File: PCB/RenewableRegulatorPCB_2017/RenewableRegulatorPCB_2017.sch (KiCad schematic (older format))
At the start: 34 parts, among them J1 JACK_TRS_6PINS, J2 Arduino_Nano_Header, P1 INPUT, P2 Vref?, P3 MicroSD, P4 A6_7, P5 OUTPUT, P6 SERIAL, P7 A2, P8 TP_Vin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

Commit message: Secod
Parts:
- C3: footprint REInnovationFootprint:C_1V7_TH -> RenewableRegulatorPCB_2017_Library_Yoan:Capacitor_C_1V7_TH
- EN1: footprint ~ -> (none)
- P1, P5: footprint matts_components:SIL-2_screw_terminal_32A -> RenewableRegulatorPCB_2017_Library_Yoan:Connecteurs_IO_SIL-2_screw_terminal_32A
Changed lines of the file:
@@
 LIBS:device
 LIBS:conn
+LIBS:RenewableRegulatorPCB_2017
 LIBS:RenewableRegulatorPCB_2017-cache
 EELAYER 25 0
@@
 F 0 "P1" V 1350 1600 40  0000 C CNN
 F 1 "INPUT" V 1450 1600 40  0000 C CNN
-F 2 "matts_components:SIL-2_screw_terminal_32A" H 1400 1600 60  0001 C CNN
+F 2 "RenewableRegulatorPCB_2017_Library_Yoan:Connecteurs_IO_SIL-2_screw_terminal_32A" H 1400 1600 60  0001 C CNN
 F 3 "" H 1400 1600 60  0001 C CNN
 	1    1400 1600
@@
 F 0 "P5" V 10200 1750 40  0000 C CNN
 F 1 "OUTPUT" V 10300 1750 40  0000 C CNN
-F 2 "matts_components:SIL-2_screw_terminal_32A" H 10250 1750 60  0001 C CNN
+F 2 "RenewableRegulatorPCB_2017_Library_Yoan:Connecteurs_IO_SIL-2_screw_terminal_32A" H 10250 1750 60  0001 C CNN
 F 3 "" H 10250 1750 60  0001 C CNN
 	1    10250 1750
@@
 F 0 "C3" H 8925 1650 50  0000 L CNN
 F 1 "100uf" H 8925 1450 50  0000 L CNN
-F 2 "REInnovationFootprint:C_1V7_TH" H 8938 1400 50  0001 C CNN
-F 3 "" H 8900 1550 50  0000 C CNN
+F 2 "RenewableRegulatorPCB_2017_Library_Yoan:Capacitor_C_1V7_TH" H 8938 1400 400 0001 C CNN
+F 3 "" H 8900 1550 400 0001 C CNN
 F 4 "~" H 8900 1550 60  0000 C CNN "Notes"
 F 5 "100V Electrolytic" H 8900 1550 60  0001 C CNN "Description"
 F 6 "Panasonic" H 8900 1550 60  0001 C CNN "Manufacturer"
-F 7 "ECA-2AM101B" H 8900 1550 60  0001 C CNN "Manufacturer Part No"
+F 7 "ECA-2AM101B" H 8900 1550 394 0001 C CNN "Manufacturer Part No"
 F 8 "RS" H 8900 1550 60  0001 C CNN "Supplier 1"
 F 9 "807-3431" H 8900 1550 60  0001 C CNN "Supplier 1 Part No"
@@
 F 0 "EN1" H 6530 6500 40  0000 L CNN
 F 1 "PCB" H 6450 6555 30  0001 C CNN
-F 2 "~" H 6450 6500 60  0001 C CNN
+F 2 "" H 6450 6500 60  0001 C CNN
 F 3 "http://cpc.farnell.com/hammond/1590bb/box-diecast-119x94x30/dp/EN82042?ost=EN82042&selectedCategoryId=&categoryNameResp=All&searchView=table&iscrfnonsku=false" H 6450 6500 60  0001 C CNN
 F 4 "~" H 6450 6500 60  0000 C CNN "Notes"

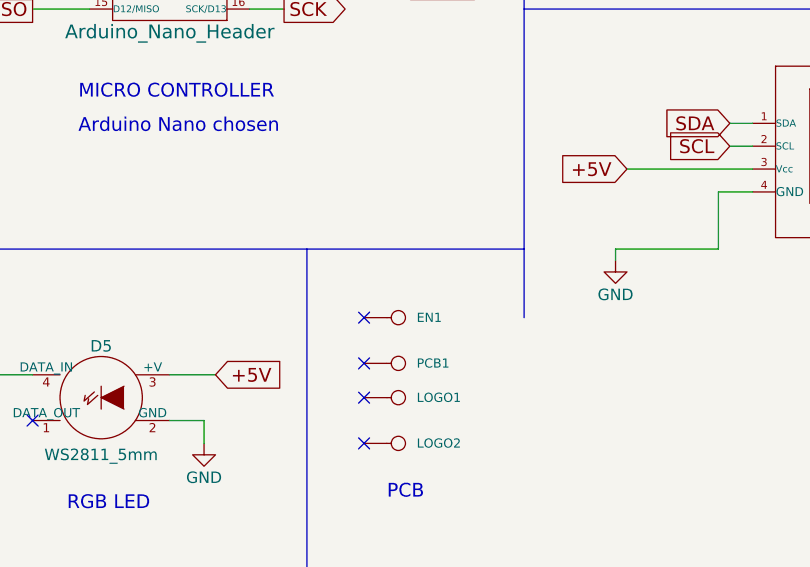
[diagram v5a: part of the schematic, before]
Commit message: Added MH and footprints
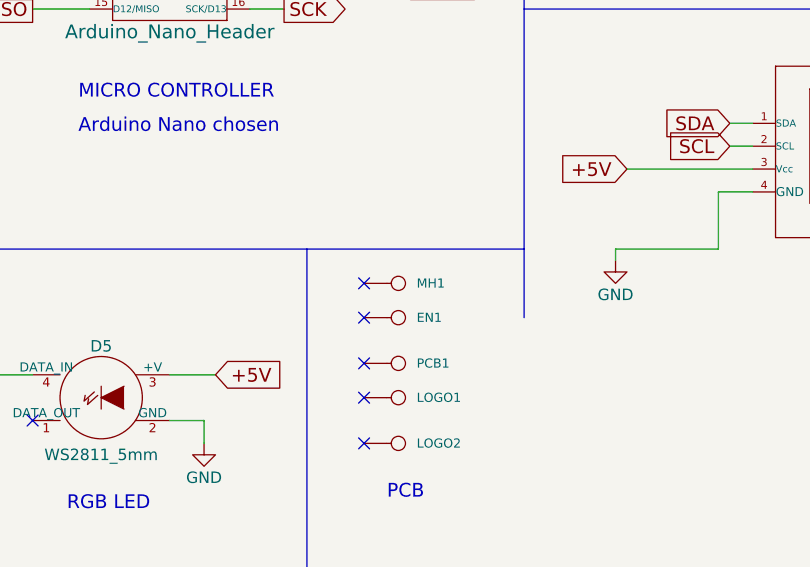
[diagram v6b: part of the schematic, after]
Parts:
- added MH1: Mounting holes, symbol CONN_1
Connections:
- no-connect marks 6 -> 7
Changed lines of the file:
@@
 LIBS:power
 LIBS:device
+LIBS:matts_components
 LIBS:conn
 LIBS:RenewableRegulatorPCB_2017
@@
 	1    0    0    -1
 $EndComp
+NoConn ~ 6300 6350
+$Comp
+L CONN_1 MH1
+U 1 1 58EBB61E
+P 6450 6350
+F 0 "MH1" H 6530 6350 40  0000 L CNN
+F 1 "Mounting holes" H 6450 6405 30  0001 C CNN
+F 2 "" H 6450 6350 60  0001 C CNN
+F 3 "" H 6450 6350 60  0001 C CNN
+F 4 "~" H 6450 6350 60  0000 C CNN "Notes"
+F 5 "4 x M3 mounting holes" H 6450 6350 60  0001 C CNN "Description"
+F 6 "~" H 6450 6350 60  0001 C CNN "Manufacturer"
+F 7 "~" H 6450 6350 60  0001 C CNN "Manufacturer Part No"
+F 8 "~" H 6450 6350 60  0001 C CNN "Supplier 1"
+F 9 "~" H 6450 6350 60  0001 C CNN "Supplier 1 Part No"
+F 10 "~" H 6450 6350 60  0001 C CNN "Supplier 1 Cost"
+F 11 "~" H 6450 6350 60  0001 C CNN "Supplier 2"
+F 12 "~" H 6450 6350 60  0001 C CNN "Supplier 2 Part No"
+F 13 "~" H 6450 6350 60  0001 C CNN "Supplier 2 Cost"
+	1    6450 6350
+	1    0    0    -1
+$EndComp

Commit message: Third Version of PCB
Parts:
- P1, P5: symbol CONN_2 -> CONN_2-RESCUE-RenewableRegulatorPCB_2017
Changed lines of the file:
@@
 LIBS:power
 LIBS:device
-LIBS:matts_components
 LIBS:conn
 LIBS:RenewableRegulatorPCB_2017
@@
 $EndComp
 $Comp
-L CONN_2 P1
+L CONN_2-RESCUE-RenewableRegulatorPCB_2017 P1
 U 1 1 50D3652B
 P 1400 1600
@@
 Reverse Polarity Protection\nWill blow control fuse if reversed.
 $Comp
-L CONN_2 P5
+L CONN_2-RESCUE-RenewableRegulatorPCB_2017 P5
 U 1 1 58E5328E
 P 10250 1750

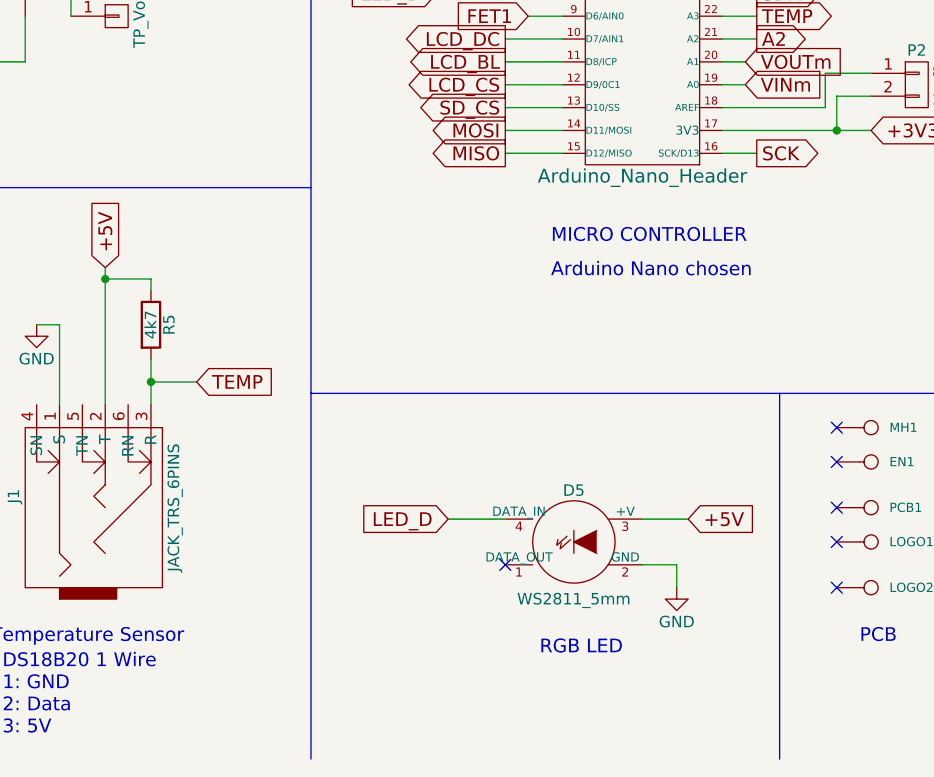
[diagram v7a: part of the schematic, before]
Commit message: Updated PCB and schematic
WS2811 LED swapped around Vcc and GND
OLED swapped around for front mounting
Tracks cleaned up
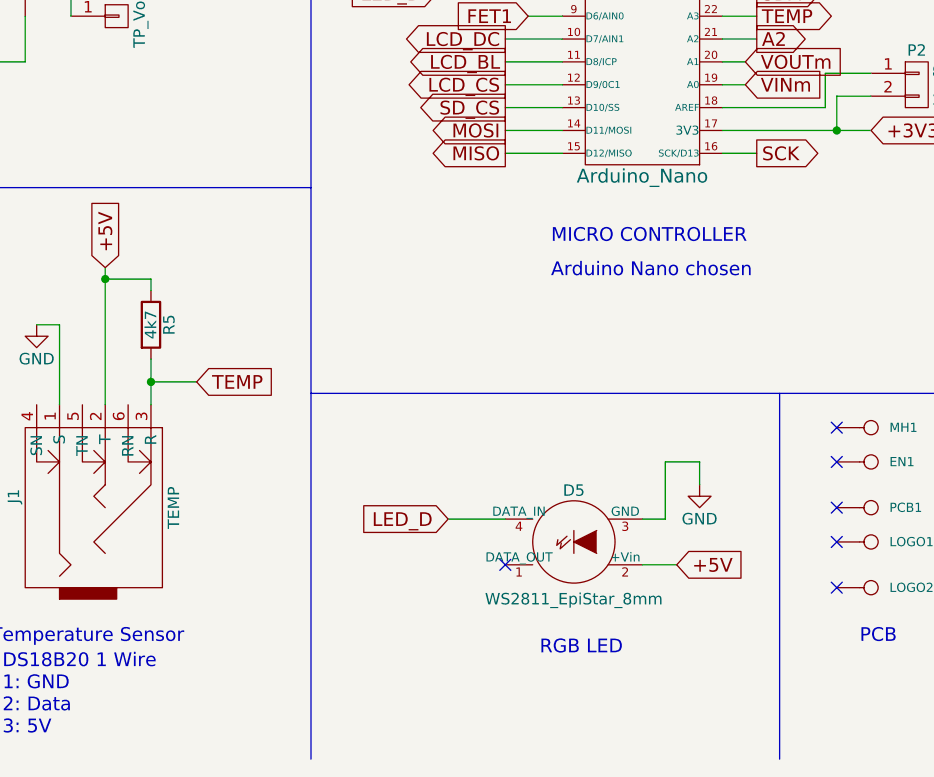
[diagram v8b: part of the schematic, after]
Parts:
- removed D5: WS2811_5mm, REInnovationFootprint:TH_WS2811_LED_8mm, symbol WS2811_5mm
- added D5: WS2811_EpiStar_8mm, REInnovationFootprint:TH_WS2811_LED_8mm, symbol WS2811_EpiStar_8mm
- J1: value JACK_TRS_6PINS -> TEMP
- J2: value Arduino_Nano_Header -> Arduino_Nano
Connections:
- net +5V: now also D5.2 (+Vin)
- net GND: now also D5.3 (GND)
- net LED_D: now also D5.4 (DATA_IN)
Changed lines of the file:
@@
 LIBS:conn
 LIBS:RenewableRegulatorPCB_2017
+LIBS:matts_components
 LIBS:RenewableRegulatorPCB_2017-cache
 EELAYER 25 0
@@
 P 5450 4450
 F 0 "J2" H 5450 5250 60  0000 C CNN
-F 1 "Arduino_Nano_Header" H 5450 3650 60  0000 C CNN
+F 1 "Arduino_Nano" H 5450 3650 60  0000 C CNN
 F 2 "REInnovationFootprint:NANO_DIP_30_600" H 5450 4450 60  0001 C CNN
 F 3 "" H 5450 4450 60  0000 C CNN
@@
 	1    0    0    -1
 $EndComp
-$Comp
-L WS2811_5mm D5
-U 1 1 58E3F557
-P 5150 6850
-F 0 "D5" H 5150 7075 50  0000 C CNN
-F 1 "WS2811_5mm" H 5150 6600 50  0000 C CNN
-F 2 "REInnovationFootprint:TH_WS2811_LED_8mm" H 5150 6850 50  0001 C CNN
-F 3 "https://www.coolcomponents.co.uk/en/opto/leds/digital-rgb-addressable-led-5mm-through-hole-10-pack.html" H 5150 6850 50  0001 C CNN
-F 4 "~" H 5150 6850 60  0000 C CNN "Notes"
-F 5 "TH WS2811 Single LED Addressable" H 5150 6850 60  0001 C CNN "Description"
-F 6 "~" H 5150 6850 60  0001 C CNN "Manufacturer"
-F 7 "~" H 5150 6850 60  0001 C CNN "Manufacturer Part No"
-F 8 "AliExpress" H 5150 6850 60  0001 C CNN "Supplier 1"
-F 9 "~" H 5150 6850 60  0001 C CNN "Supplier 1 Part No"
-F 10 "~" H 5150 6850 60  0001 C CNN "Supplier 1 Cost"
-F 11 "~" H 5150 6850 60  0001 C CNN "Supplier 2"
-F 12 "~" H 5150 6850 60  0001 C CNN "Supplier 2 Part No"
-F 13 "~" H 5150 6850 60  0001 C CNN "Supplier 2 Cost"
-	1    5150 6850
-	1    0    0    -1
-$EndComp
 Wire Wire Line
 	5500 2100 6300 2100
@@
 Wire Wire Line
 	5500 2300 5750 2300
-Text GLabel 5650 6750 2    60   Input ~ 0
+Text GLabel 5600 6950 2    60   Input ~ 0
 +5V
 Wire Wire Line
-	5450 6750 5650 6750
-Wire Wire Line
-	5450 6950 5600 6950
-Wire Wire Line
-	5600 6950 5600 7050
+	5700 6500 5700 6600
 Text GLabel 7450 5850 0    60   Input ~ 0
 +5V
@@
 L GND #PWR05
 U 1 1 58E495BD
-P 5600 7050
-F 0 "#PWR05" H 5600 6800 50  0001 C CNN
-F 1 "GND" H 5600 6900 50  0000 C CNN
-F 2 "" H 5600 7050 50  0000 C CNN
-F 3 "" H 5600 7050 50  0000 C CNN
-	1    5600 7050
+P 5700 6600
+F 0 "#PWR05" H 5700 6350 50  0001 C CNN
+F 1 "GND" H 5700 6450 50  0000 C CNN
+F 2 "" H 5700 6600 50  0000 C CNN
+F 3 "" H 5700 6600 50  0000 C CNN
+	1    5700 6600
 	1    0    0    -1
 $EndComp
@@
 P 3100 6650
 F 0 "J1" H 3100 7050 50  0000 C CNN
-F 1 "JACK_TRS_6PINS" H 3050 6350 50  0000 C CNN
+F 1 "TEMP" H 3050 6350 50  0000 C CNN
 F 2 "REInnovationFootprint:TH_3_5mm_Jack" H 3200 6500 50  0001 C CNN
 F 3 "" H 3200 6500 50  0000 C CNN
@@
 	1    0    0    -1
 $EndComp
+$Comp
+L WS2811_EpiStar_8mm D5
+U 1 1 58F0DF7B
+P 5150 6850
+F 0 "D5" H 5150 7075 50  0000 C CNN
+F 1 "WS2811_EpiStar_8mm" H 5150 6600 50  0000 C CNN
+F 2 "REInnovationFootprint:TH_WS2811_LED_8mm" H 5150 6850 50  0001 C CNN
+F 3 "" H 5150 6850 50  0000 C CNN
+	1    5150 6850
+	1    0    0    -1
+$EndComp
+Wire Wire Line
+	5450 6950 5600 6950
+Wire Wire Line
+	5450 6750 5550 6750
+Wire Wire Line
+	5550 6750 5550 6500
+Wire Wire Line
+	5550 6500 5700 6500
 $EndSCHEMATC
